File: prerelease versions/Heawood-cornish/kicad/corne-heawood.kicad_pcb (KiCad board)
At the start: 2 copper layers, 133.8 x 91.4 mm, 56 parts, among them J1 OLED, SW1 SW_PUSH, SW10 SW_PUSH, SW11 SW_PUSH, SW12 SW_PUSH, SW13 SW_PUSH, SW14 SW_PUSH, SW15 SW_PUSH, SW16 SW_PUSH, SW17 SW_PUSH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

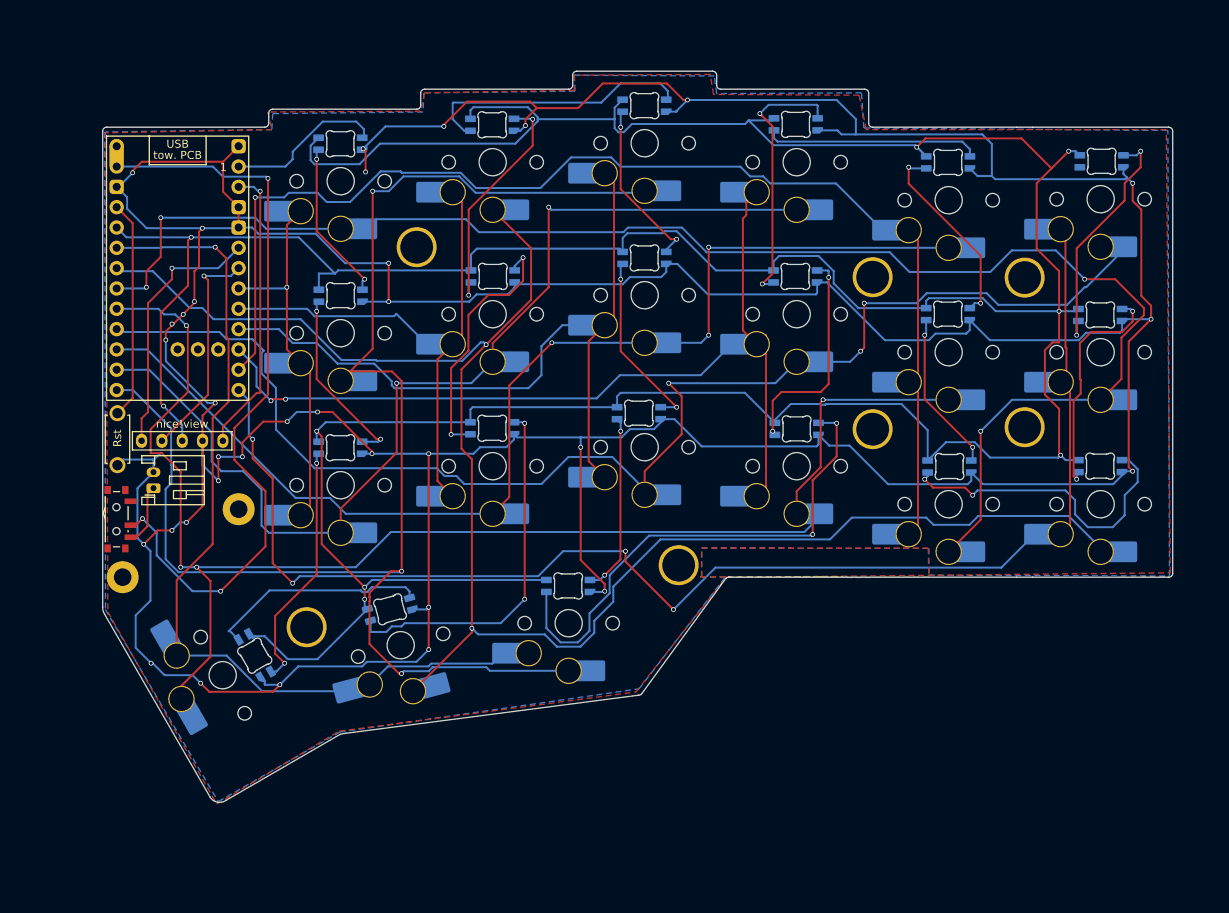
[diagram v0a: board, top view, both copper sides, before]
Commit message: Add QMK firmware files
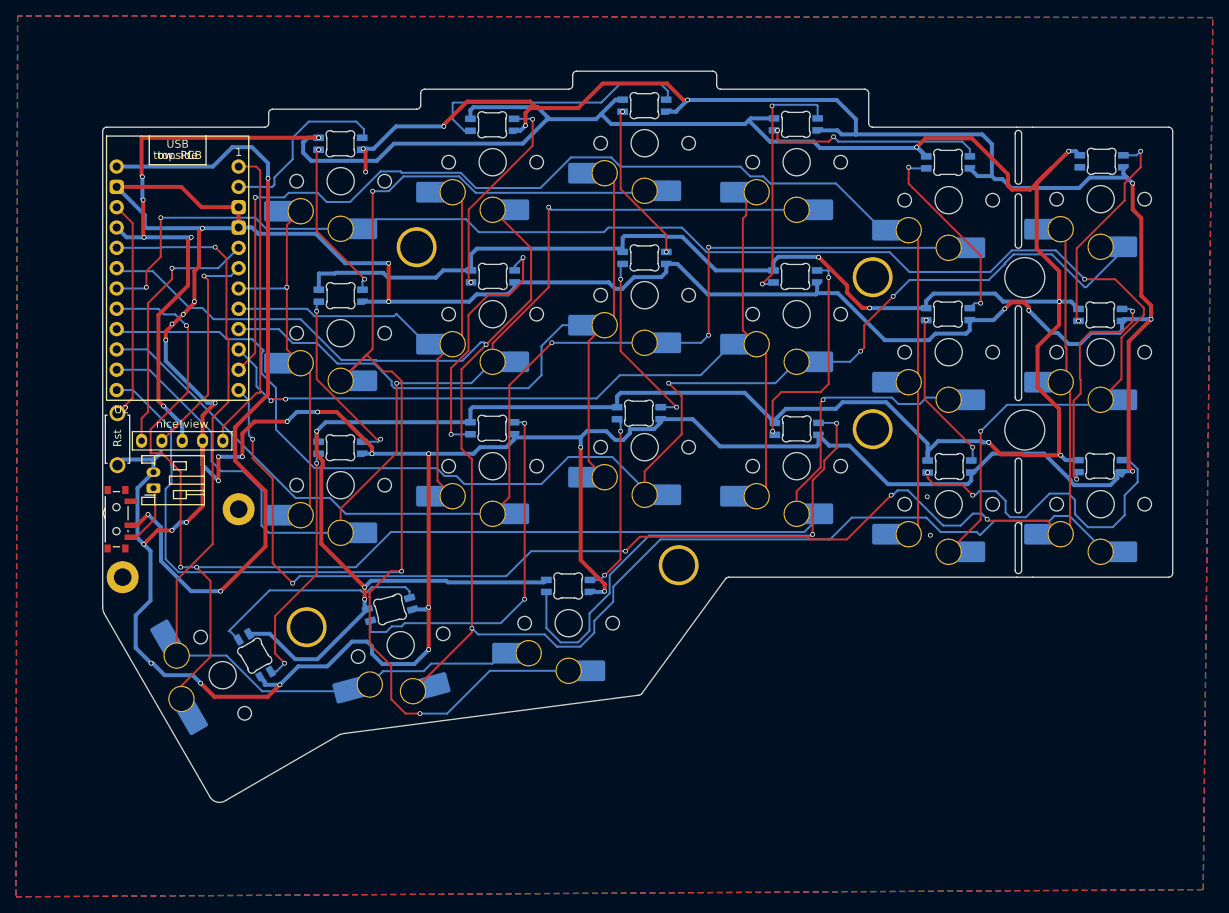
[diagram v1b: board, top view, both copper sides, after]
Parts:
- removed the ? at (180.2, 105.5)
- removed the ? at (180.2, 86.8)
- U2: footprint PCM_marbastlib-xp-promicroish:nice_nano_AH_Reversible -> PCM_marbastlib-xp-promicroish:ProMicro_USBdn; moved to F.Cu
- turned U2 to 0 degrees
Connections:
- U2 pad 1: LED -> CS
- U2 pad 2: CS -> LED
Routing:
- net VCC: track 513.9 -> 533.8 mm, vias 9 -> 16
- net row0: track 191.6 -> 199.6 mm
- net GND: track 666.5 -> 671.5 mm, vias 34 -> 37
- net +BATT: track 93.8 -> 98.1 mm
- net Net-(LED1-DIN): track 30.6 -> 27.0 mm
- net Net-(LED11-DOUT): track 29.4 -> 26.2 mm
- net LED: track 20.0 -> 22.6 mm
- net Net-(LED13-DIN): track 39.5 -> 42.1 mm
- net CS: track 36.3 -> 38.9 mm, vias 1 -> 0
- net col0: track 168.7 -> 171.2 mm, vias 4 -> 5
- net Net-(LED3-DIN): track 33.3 -> 31.7 mm
- net Net-(LED10-DIN): track 21.5 -> 20.0 mm
- net row6: track 212.6 -> 213.7 mm
- net row4: track 180.4 -> 181.3 mm
- net row3: track 165.0 -> 165.6 mm
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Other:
- outline, holes or cut-outs redrawn
